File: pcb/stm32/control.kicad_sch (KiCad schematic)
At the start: 29 parts, among them J1 USB_C_Receptacle_USB2.0, J4 Term, P1 ST-Link, P2 ST-Link, P3 UG-2864ASWPG01, P4 har-flexicon 2,54 MSH-4, P5 WAGO2061-602, SW1 RotaryEncoder_Switch, U1 STM32G431CBUx, U3 BME680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

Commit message: Cleanup, add casing
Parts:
- removed R10: 10k, Resistor_SMD:R_0603_1608Metric, symbol Device:R
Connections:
- net SW: no longer U1.30 (PA8)
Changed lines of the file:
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@@
   (junction (at 38.1 182.245) (diameter 0) (color 0 0 0 0)
   )
-  (junction (at 143.51 58.42) (diameter 0) (color 0 0 0 0)
-  )
   (junction (at 33.02 97.79) (diameter 0) (color 0 0 0 0)
   )
@@
     (stroke (width 0) (type default))
   )
-  (wire (pts (xy 143.51 58.42) (xy 145.415 58.42))
-    (stroke (width 0) (type default))
-  )
   (wire (pts (xy 219.71 50.8) (xy 219.71 52.07))
     (stroke (width 0) (type default))
@@
     (stroke (width 0) (type default))
   )
-  (wire (pts (xy 143.51 58.42) (xy 143.51 60.325))
-    (stroke (width 0) (type default))
-  )
   (wire (pts (xy 197.485 146.05) (xy 208.28 146.05))
     (stroke (width 0) (type default))
@@
   )
   (wire (pts (xy 260.35 100.965) (xy 259.08 100.965))
-    (stroke (width 0) (type default))
-  )
-  (wire (pts (xy 120.015 58.42) (xy 143.51 58.42))
     (stroke (width 0) (type default))
   )
@@
     (effects (font (size 1.27 1.27)) (justify left bottom))
   )
-  (text "BOOT0" (at 135.255 57.785 0)
+  (text "BOOT0" (at 67.31 97.79 0)
     (effects (font (size 1.27 1.27)) (justify left bottom))
   )
@@
   (text "ST-Link" (at 273.05 128.27 0)
     (effects (font (size 1.27 1.27)) (justify left bottom))
-  )
-  (global_label "SW" (shape input) (at 145.415 58.42 0) (fields_autoplaced)
-    (effects (font (size 1.27 1.27)) (justify left))
-    (property "Intersheetrefs" "${INTERSHEET_REFS}" (at 151.0611 58.42 0)
-      (effects (font (size 1.27 1.27)) (justify left) hide)
-    )
   )
   (global_label "nRST" (shape input) (at 274.32 140.335 180) (fields_autoplaced)
@@
     )
   )
-  (symbol (lib_id "power:GND") (at 143.51 67.945 0) (unit 1)
-    (in_bom yes) (on_board yes) (dnp no)
-    (property "Reference" "#PWR015" (at 143.51 74.295 0)
-      (effects (font (size 1.27 1.27)) hide)
-    )
-    (property "Value" "GND" (at 143.51 71.755 0)
-      (effects (font (size 1.27 1.27)))
-    )
-    (property "Footprint" "" (at 143.51 67.945 0)
-      (effects (font (size 1.27 1.27)))
-    )
-    (property "Datasheet" "" (at 143.51 67.945 0)
-      (effects (font (size 1.27 1.27)))
-    )
-    (pin "1")
-    (instances
-      (project "control"
-        (path "/4b540715-c4ed-4902-8525-92fb403f6b2e"
-          (reference "#PWR015") (unit 1)
-        )
-      )
-      (project "LedControl"
-        (path "/985c599b-be96-45f9-a3b4-3f0067b0d733"
-          (reference "#PWR01") (unit 1)
-        )
-      )
-    )
-  )
   (symbol (lib_id "power:GND") (at 210.82 162.56 0) (unit 1)
     (in_bom yes) (on_board yes) (dnp no) (fields_autoplaced)
@@
         )
       )
-    )
-  )
-  (symbol (lib_id "Device:R") (at 143.51 64.135 0) (unit 1)
-    (in_bom yes) (on_board yes) (dnp no)
-    (property "Reference" "R10" (at 145.288 62.9666 0)
-      (effects (font (size 1.27 1.27)) (justify left))
-    )
-    (property "Value" "10k" (at 145.288 65.278 0)
-      (effects (font (size 1.27 1.27)) (justify left))
-    )
-    (property "Footprint" "Resistor_SMD:R_0603_1608Metric" (at 141.732 64.135 90)
-      (effects (font (size 1.27 1.27)) hide)
-    )
-    (property "Datasheet" "~" (at 143.51 64.135 0)
-      (effects (font (size 1.27 1.27)) hide)
-    )
-    (pin "1")
-    (pin "2")
-    (instances
-      (project "control"
-        (path "/19a3d4e9-68c8-4ed7-8e07-9dbe1787e960"
-          (reference "R10") (unit 1)
-        )
-      )
-      (project "Display"
-        (path "/1d03a724-b61f-4021-9dcb-6a5edf10ce9e"
-          (reference "R1") (unit 1)
-        )
-      )
-      (project "control"
-        (path "/4b540715-c4ed-4902-8525-92fb403f6b2e"
-          (reference "R1") (unit 1)
-        )
-      )

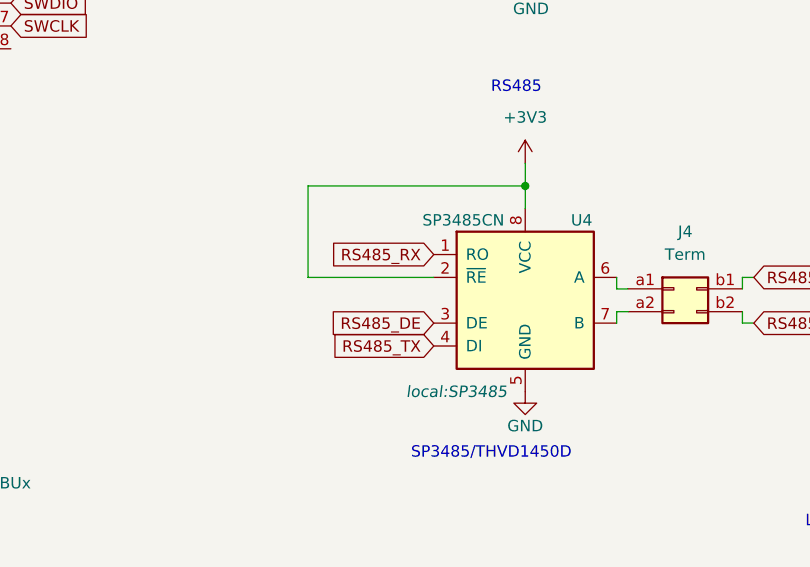
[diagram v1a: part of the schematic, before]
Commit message: Control brightness and duraton with remote control
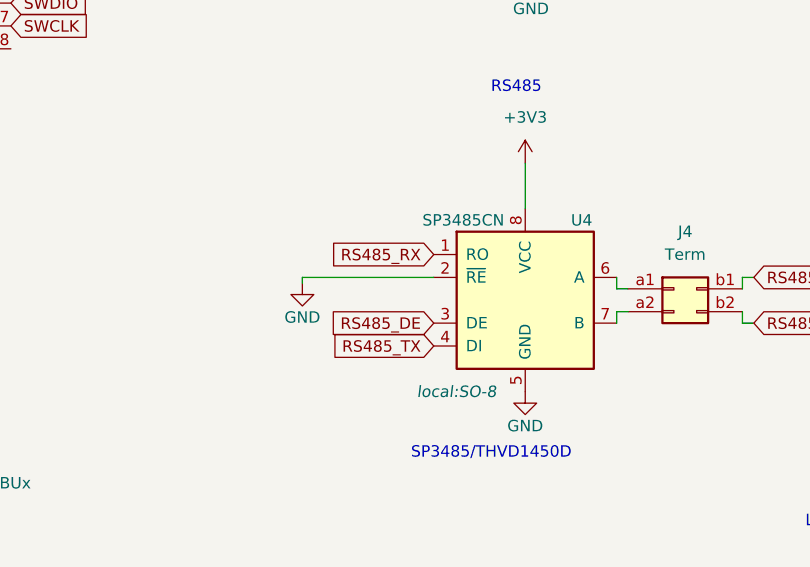
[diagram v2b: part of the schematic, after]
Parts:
- U4: footprint local:SP3485 -> local:SO-8
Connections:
- net +3V3: no longer U4.2 (~{RE})
- net GND: now also U4.2 (~{RE})
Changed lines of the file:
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@@
   (junction (at 33.02 67.31) (diameter 0) (color 0 0 0 0)
   )
-  (junction (at 177.165 91.44) (diameter 0) (color 0 0 0 0)
-  )
   (junction (at 38.1 182.245) (diameter 0) (color 0 0 0 0)
   )
@@
     (stroke (width 0) (type default))
   )
-  (wire (pts (xy 177.165 91.44) (xy 177.165 93.98))
-    (stroke (width 0) (type default))
-  )
   (wire (pts (xy 48.26 167.005) (xy 54.61 167.005))
     (stroke (width 0) (type default))
@@
     (stroke (width 0) (type default))
   )
+  (wire (pts (xy 152.4 102.235) (xy 152.4 101.6))
+    (stroke (width 0) (type default))
+  )
   (wire (pts (xy 34.29 149.225) (xy 40.64 149.225))
     (stroke (width 0) (type default))
@@
     (stroke (width 0) (type default))
   )
-  (wire (pts (xy 153.035 91.44) (xy 177.165 91.44))
-    (stroke (width 0) (type default))
-  )
   (wire (pts (xy 31.75 105.41) (xy 40.64 105.41))
     (stroke (width 0) (type default))
@@
     (stroke (width 0) (type default))
   )
-  (wire (pts (xy 153.035 91.44) (xy 153.035 101.6))
-    (stroke (width 0) (type default))
-  )
   (wire (pts (xy 208.28 160.02) (xy 208.28 146.05))
     (stroke (width 0) (type default))
@@
     (stroke (width 0) (type default))
   )
-  (wire (pts (xy 167.005 101.6) (xy 153.035 101.6))
+  (wire (pts (xy 152.4 101.6) (xy 167.005 101.6))
     (stroke (width 0) (type default))
   )
@@
     (stroke (width 0) (type default))
   )
-  (wire (pts (xy 177.165 88.9) (xy 177.165 91.44))
+  (wire (pts (xy 177.165 88.9) (xy 177.165 93.98))
     (stroke (width 0) (type default))
   )
@@
       (effects (font (size 1.27 1.27)) (justify left))
     )
-    (property "Footprint" "local:SP3485" (at 169.545 114.3 0)
+    (property "Footprint" "local:SO-8" (at 169.545 114.3 0)
       (effects (font (size 1.27 1.27) italic))
     )
@@
         )
       )
+    )
+  )
+  (symbol (lib_id "power:GND") (at 152.4 102.235 0) (unit 1)
+    (in_bom yes) (on_board yes) (dnp no)
+    (property "Reference" "#PWR015" (at 152.4 108.585 0)
+      (effects (font (size 1.27 1.27)) hide)
+    )
+    (property "Value" "GND" (at 152.4 106.045 0)
+      (effects (font (size 1.27 1.27)))
+    )
+    (property "Footprint" "" (at 152.4 102.235 0)
+      (effects (font (size 1.27 1.27)))
+    )
+    (property "Datasheet" "" (at 152.4 102.235 0)
+      (effects (font (size 1.27 1.27)))
+    )
+    (pin "1")
+    (instances
+      (project "control"
+        (path "/4b540715-c4ed-4902-8525-92fb403f6b2e"
+          (reference "#PWR015") (unit 1)
+        )
+      )
+      (project "LedControl"
+        (path "/985c599b-be96-45f9-a3b4-3f0067b0d733"
+          (reference "#PWR01") (unit 1)
+        )
+      )

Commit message: Add SnowSparkle, new footprints
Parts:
- removed P1: ST-Link, local:FTSH-107-01-L-DV-K, symbol Connector_Generic:Conn_01x14
- added P1: FTSH-107-01-L-DV-K, local:PinHeader-2x7-1.27mm-smd, symbol Connector_Generic:Conn_02x07_Odd_Even
- P3: footprint local:Connector-Flat-24_P0.5mm -> local:Connector-Flat-24-0.5mm
- renumbered C3 to C1, C3 to C2, R10 to R1, R1 to R4, R2 to R5, U7 to U2
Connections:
- net +3V3: now also P1.3 (Pin_3)
- net GND: now also P1.5 (Pin_5), P1.7 (Pin_7)
- net SWCLK: now also P1.6 (Pin_6)
- net SWDIO: now also P1.4 (Pin_4)
- net VCP_RX: now also P1.13 (Pin_13)
- net VCP_TX: now also P1.14 (Pin_14)
- net nRST: now also P1.12 (Pin_12)
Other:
- moved on the sheet: D4, P4, P5
